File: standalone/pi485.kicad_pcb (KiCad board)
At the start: 2 copper layers, 63 x 46 mm, 29 parts, among them J1 RS485, P1 Rasperry Pi, P2 PWR, P3 Term, P4 Latch Disable, Q1 2N4401, Q2 2N4401, Q3 2N4401, U1 NE555, U2 MAX485

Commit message: Updated Plots
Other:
- board text added: "Pi485 Rev 1.1.0"
- board text removed: "Pi485 Rev 1.1.0 2017-1-18"
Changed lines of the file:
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@@
       (padsonsilk true)
       (subtractmaskfromsilk false)
-      (outputformat 4)
+      (outputformat 5)
       (mirror false)
       (drillshape 1)
@@
     (effects (font (size 1.25 1.25) (thickness 0.2)))
   )
-  (gr_text "Pi485\nRev 1.1.0\n2017-1-18" (at 25.341 19.34) (layer F.SilkS)
+  (gr_text "Pi485\nRev 1.1.0" (at 25.341 18.15) (layer F.SilkS)
     (effects (font (size 1.5 1.5) (thickness 0.3)))
   )

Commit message: Esthetics on the standalone board.
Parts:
- moved Q3 4.67 mm to (21.5, 38.5)
- moved R5 4.45 mm to (30.4, 31.4)
- moved R6 3.50 mm to (26.3, 35.8)
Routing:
- net Net-(J1-Pad2): track 30.5 -> 35.4 mm
- net Net-(J1-Pad1): track 30.7 -> 35.5 mm
- net Net-(P3-Pad1): track 14.4 -> 9.95 mm
- net VCC: track 31.5 -> 27.6 mm
- net Net-(Q3-Pad2): track 21.9 -> 19.8 mm
- net Net-(C1-Pad1): track 134.0 -> 134.9 mm

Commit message: Symmetry is beautiful.
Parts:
- RO: renamed from P4; value Latch Disable -> RO
- moved C3 2.97 mm to (56.8, 24.4), turned to 90 degrees
- moved Term 2.91 mm to (26.2, 25.4)
- moved RO 1.77 mm to (60.6, 20.7), turned to 0 degrees
- renumbered P3 to Term
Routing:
- net GND: track 192.2 -> 188.4 mm
- net Net-(P3-Pad1): track 9.95 -> 7.32 mm
- net Net-(U1-Pad3): track 32.2 -> 34.3 mm
- net Net-(P4-Pad2): track 11.5 -> 13.5 mm
- net Net-(C1-Pad1): track 134.9 -> 133.8 mm
- net Net-(J1-Pad1): track 35.5 -> 34.4 mm

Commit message: Some additional cleanup and re-routing
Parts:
- removed MNT01, MNT02: MountingHole_3.7mm_Pad, Mounting_Holes:MountingHole_3.7mm_Pad
- removed RO: RO, Pin_Headers:Pin_Header_Straight_1x02
- removed Term: Term, Pin_Headers:Pin_Header_Straight_1x02
- added P3: Term, Pin_Headers:Pin_Header_Straight_1x02, F.Cu at (26.3, 25.1)
- added P4: RO, Pin_Headers:Pin_Header_Straight_1x02, F.Cu at (60.6, 20.7)
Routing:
- net GND: track 188.4 -> 191.8 mm
- net Net-(P3-Pad1): track 7.32 -> 6.78 mm

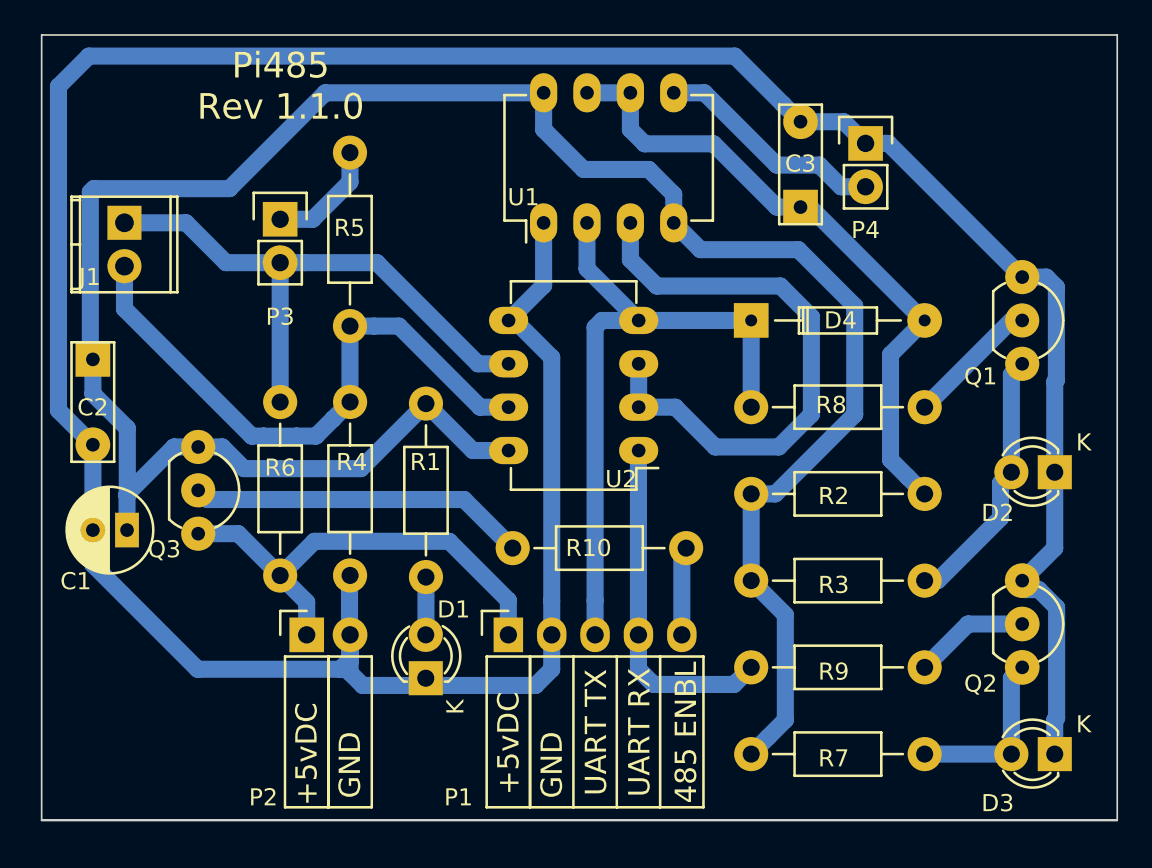
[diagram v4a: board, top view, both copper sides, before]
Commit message: Low-side NPN switching. We'll see if things 'floating' causes issues... if so, I'll have to order a few PNP's to use for high-side switching.
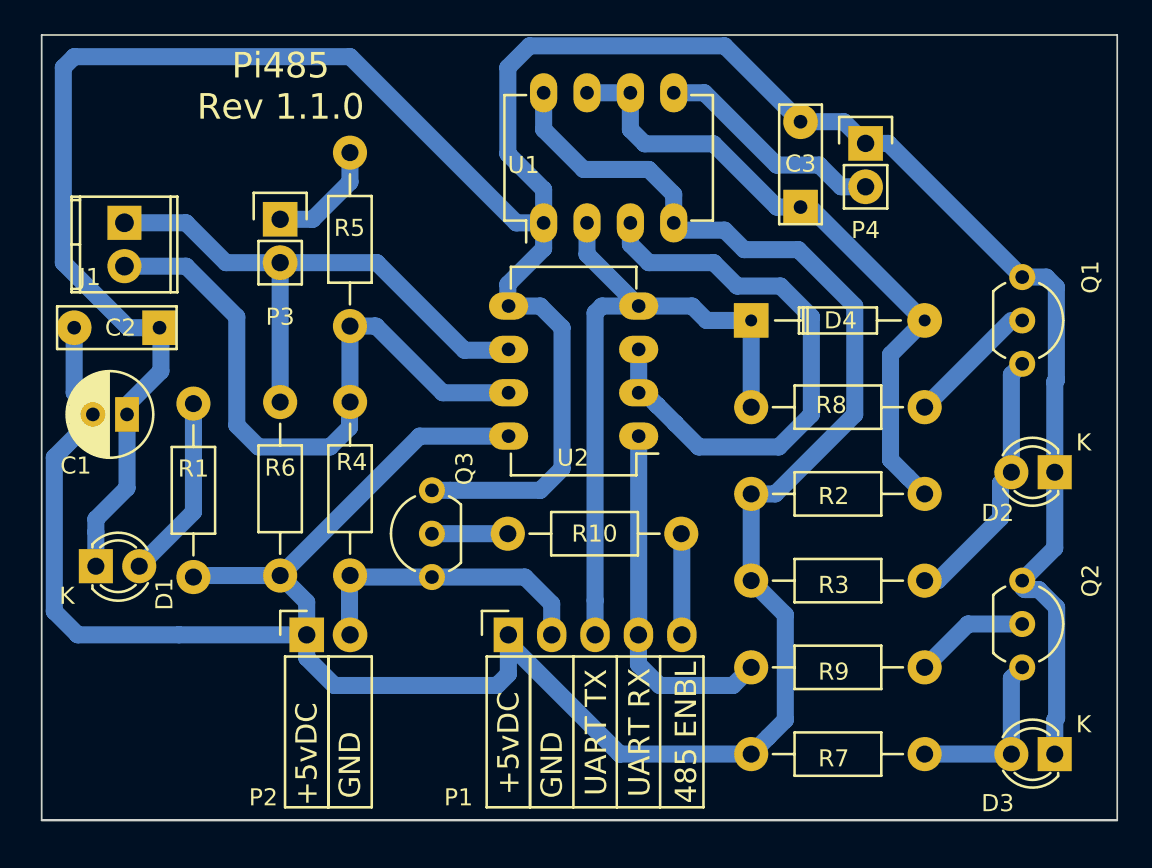
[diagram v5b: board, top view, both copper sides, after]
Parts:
- P3: value Term -> TERM
- moved D1 20.4 mm to (15.5, 45.5), turned to 0 degrees
- moved R1 17.0 mm to (21.2, 35.9), turned to 270 degrees
- moved Q3 15.7 mm to (35.2, 46.1), turned to 90 degrees
- moved C1 6.78 mm to (17.3, 36.6)
- moved C2 4.32 mm to (19.2, 31.5), turned to 180 degrees
- moved R10 0.89 mm to (39.6, 43.5)
- moved U2 0.84 mm to (47.3, 37.8)
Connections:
- C1 pad 2: GND -> VCC
- C2 pad 2: GND -> VCC
- C3 pad 2: GND -> Net-(C1-Pad1)
- D1 pad 1: GND -> Net-(C1-Pad1)
- D2 pad 1: GND -> Net-(C1-Pad1)
- D3 pad 1: GND -> Net-(C1-Pad1)
- P4 pad 1: GND -> Net-(C1-Pad1)
- Q1 pad 1: Net-(D2-Pad2) -> Net-(C1-Pad1)
- Q1 pad 3: GND -> Net-(D2-Pad2)
- Q2 pad 1: Net-(D3-Pad2) -> Net-(C1-Pad1)
- Q2 pad 3: GND -> Net-(D3-Pad2)
- Q3 pad 1: VCC -> GND
- R1 pad 2: Net-(C1-Pad1) -> VCC
- R2 pad 2: Net-(C1-Pad1) -> VCC
- R3 pad 2: Net-(C1-Pad1) -> VCC
- R7 pad 2: Net-(C1-Pad1) -> VCC
- U1 pad 1: GND -> Net-(C1-Pad1)
- U1 pad 4: Net-(C1-Pad1) -> VCC
- U1 pad 8: Net-(C1-Pad1) -> VCC
- U2 pad 5: GND -> Net-(C1-Pad1)
- U2 pad 8: Net-(C1-Pad1) -> VCC
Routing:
- net GND: track 191.8 -> 18.6 mm
- net VCC: track 27.6 -> 150.5 mm
- net Net-(C1-Pad1): track 133.8 -> 169.9 mm
- net Net-(Q3-Pad2): track 19.8 -> 4.45 mm
- net Net-(D1-Pad2): track 3.39 -> 10.8 mm
- net Net-(J1-Pad2): track 35.4 -> 38.6 mm
- net /(485PWR)_GPIO18: track 5.19 -> 5.94 mm
- net /(RXDO)_GPIO15: track 20.2 -> 20.9 mm
- net Net-(J1-Pad1): track 34.7 -> 34.0 mm
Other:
- rule via_min_drill: 0.8 -> 0.4

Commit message: Updated standalone for asthetics.
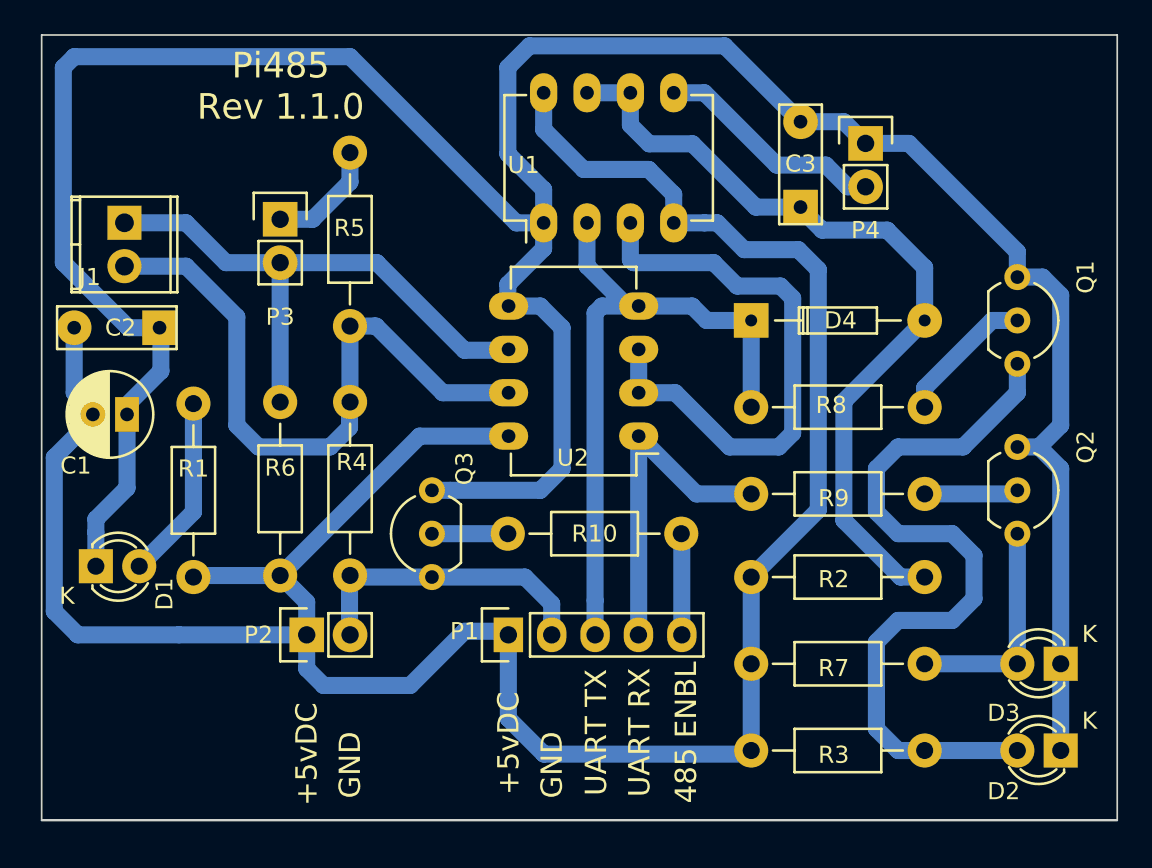
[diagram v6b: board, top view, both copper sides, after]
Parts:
- P1: footprint Socket_Strips:Socket_Strip_Angled_1x05 -> Pin_Headers:Pin_Header_Straight_1x05
- P2: footprint Socket_Strips:Socket_Strip_Angled_1x02 -> Pin_Headers:Pin_Header_Straight_1x02
- moved D2 16.3 mm to (72.0, 56.2)
- moved R9 10.2 mm to (64.1, 41.2)
- moved R3 9.95 mm to (64.1, 56.2)
- moved Q2 7.84 mm to (69.5, 38.5)
- moved D3 5.30 mm to (72.0, 51.2)
- moved R7 5.29 mm to (64.1, 51.2)
- moved R2 4.87 mm to (64.1, 46.1)
- moved Q1 0.28 mm to (69.5, 28.5)
- turned P1 to 90 degrees
- turned P2 to 90 degrees
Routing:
- net Net-(D2-Pad2): track 15.5 -> 44.3 mm
- net Net-(C3-Pad1): track 38.4 -> 48.0 mm
- net Net-(D3-Pad2): track 10.4 -> 13.0 mm
- net VCC: track 150.5 -> 148.0 mm
- net Net-(Q2-Pad2): track 7.13 -> 5.52 mm
- net /(RXDO)_GPIO15: track 20.9 -> 19.6 mm
- net Net-(Q1-Pad2): track 7.18 -> 8.20 mm
- net Net-(C1-Pad1): track 169.9 -> 170.7 mm

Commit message: standalone reconfigured for high-side PNP switching
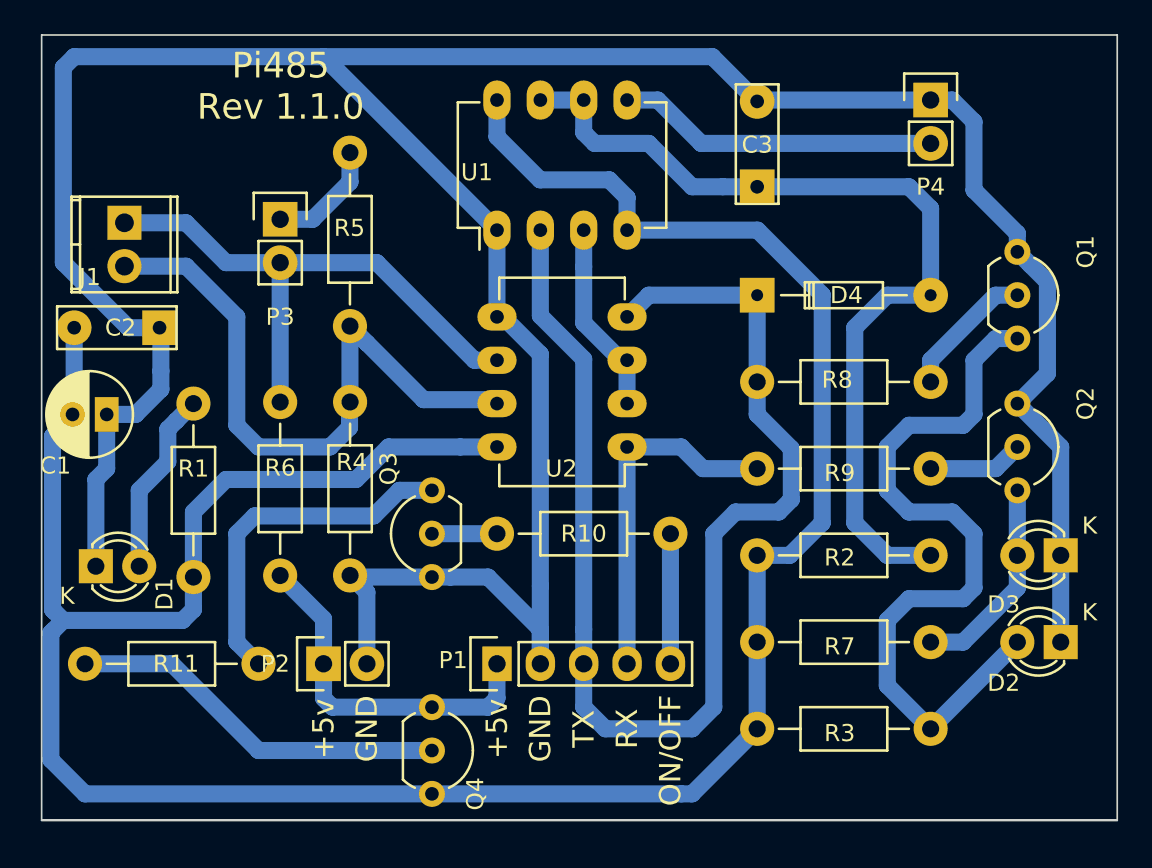
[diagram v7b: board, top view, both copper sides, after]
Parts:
- added Q4: 2N3906, TO_SOT_Packages_THT:TO-92_Inline_Wide, F.Cu at (35.2, 53.7)
- added R11: 270, Resistors_THT:Resistor_Horizontal_RM10mm, F.Cu at (14.9, 51.2)
- Q1, Q2, Q3: value 2N4401 -> 2N3904
- moved D2 6.35 mm to (72.0, 49.9)
- moved D3 6.35 mm to (72.0, 44.8)
- moved P4 4.58 mm to (64.4, 18.1)
- moved C3 2.80 mm to (54.3, 23.2)
- moved U1 2.77 mm to (39.0, 25.8)
- moved Q2 2.54 mm to (69.5, 35.9)
- moved P2 1.96 mm to (28.9, 51.2)
- moved P1 1.82 mm to (39.0, 51.2)
- moved R8 1.52 mm to (64.4, 34.7)
- moved D4 1.52 mm to (54.3, 29.6)
- moved R9 1.52 mm to (64.4, 39.7)
- moved Q1 1.48 mm to (69.5, 27.0)
- moved R2 1.32 mm to (64.4, 44.8)
- moved R3 1.32 mm to (64.4, 55.0)
- moved R7 1.32 mm to (64.4, 49.9)
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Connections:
- C1 pad 1: Net-(C1-Pad1) -> GND
- C1 pad 2: VCC -> Net-(C1-Pad2)
- C2 pad 1: Net-(C1-Pad1) -> GND
- C2 pad 2: VCC -> Net-(C1-Pad2)
- C3 pad 2: Net-(C1-Pad1) -> GND
- D1 pad 1: Net-(C1-Pad1) -> GND
- D2 pad 1: Net-(C1-Pad1) -> GND
- D3 pad 1: Net-(C1-Pad1) -> GND
- P4 pad 1: Net-(C1-Pad1) -> GND
- Q1 pad 1: Net-(C1-Pad1) -> GND
- Q2 pad 1: Net-(C1-Pad1) -> GND
- Q3 pad 3: Net-(C1-Pad1) -> Net-(Q3-Pad3)
- R1 pad 2: VCC -> Net-(C1-Pad2)
- R2 pad 2: VCC -> Net-(C1-Pad2)
- R3 pad 2: VCC -> Net-(C1-Pad2)
- R7 pad 2: VCC -> Net-(C1-Pad2)
- U1 pad 1: Net-(C1-Pad1) -> GND
- U1 pad 4: VCC -> Net-(C1-Pad2)
- U1 pad 8: VCC -> Net-(C1-Pad2)
- U2 pad 5: Net-(C1-Pad1) -> GND
- U2 pad 8: VCC -> Net-(C1-Pad2)
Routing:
- net Net-(C1-Pad1): track 170.7 -> 0.00 mm
- net GND: track 18.6 -> 185.8 mm
- net Net-(C1-Pad2): track 0.00 -> 157.5 mm
- net VCC: track 148.0 -> 20.8 mm
- net /(TXDO)_GPIO14: track 40.2 -> 74.1 mm
- net Net-(Q4-Pad2): track 0.00 -> 22.4 mm
- net Net-(U1-Pad3): track 33.7 -> 11.4 mm
- net Net-(Q3-Pad3): track 0.00 -> 20.6 mm
- net Net-(C3-Pad1): track 48.0 -> 53.6 mm
- net Net-(P4-Pad2): track 13.5 -> 18.8 mm
- net /(485PWR)_GPIO18: track 5.94 -> 7.62 mm
- net /(RXDO)_GPIO15: track 19.6 -> 20.8 mm
- net Net-(D3-Pad2): track 13.0 -> 12.1 mm
- net Net-(Q3-Pad2): track 4.45 -> 3.81 mm
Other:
- board text added: "+5v"
- board text added: "ON/OFF"
- board text added: "RX"
- board text added: "TX"
- board text removed: "+5vDC"
- board text removed: "485 ENBL"
- board text removed: "UART RX"
- board text removed: "UART TX"

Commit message: Esthetics and what-not...
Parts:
- moved P2 10.2 mm to (39.0, 51.2)
- moved Q4 7.18 mm to (30.1, 48.6)
- moved P1 3.81 mm to (39.0, 55.0)
- moved R5 2.00 mm to (30.4, 33.4)
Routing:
- net /(TXDO)_GPIO14: track 74.1 -> 87.8 mm
- net Net-(C1-Pad2): track 157.5 -> 163.0 mm
- net Net-(Q4-Pad2): track 22.4 -> 17.3 mm
- net Net-(J1-Pad2): track 38.3 -> 34.4 mm
- net /(RXDO)_GPIO15: track 20.8 -> 24.7 mm
- net /(485PWR)_GPIO18: track 7.62 -> 11.4 mm
- net Net-(P3-Pad1): track 6.78 -> 4.67 mm
- net VCC: track 20.8 -> 18.7 mm
- net GND: track 185.8 -> 184.1 mm
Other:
- board text added: "PWR"
- board text removed: "ON/OFF"
